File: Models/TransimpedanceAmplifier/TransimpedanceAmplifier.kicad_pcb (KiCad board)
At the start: 2 copper layers, 12 parts

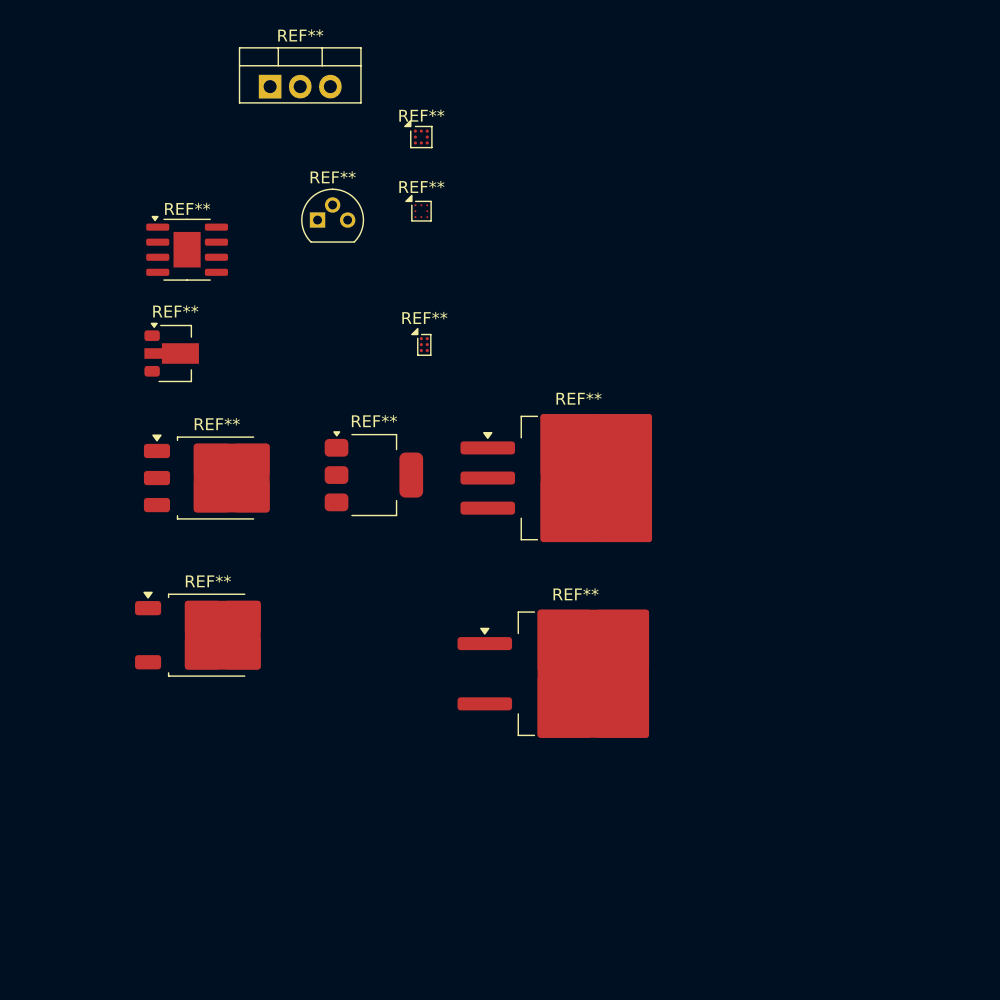
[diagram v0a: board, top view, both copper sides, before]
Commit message: Added KiCad libraries for more chips
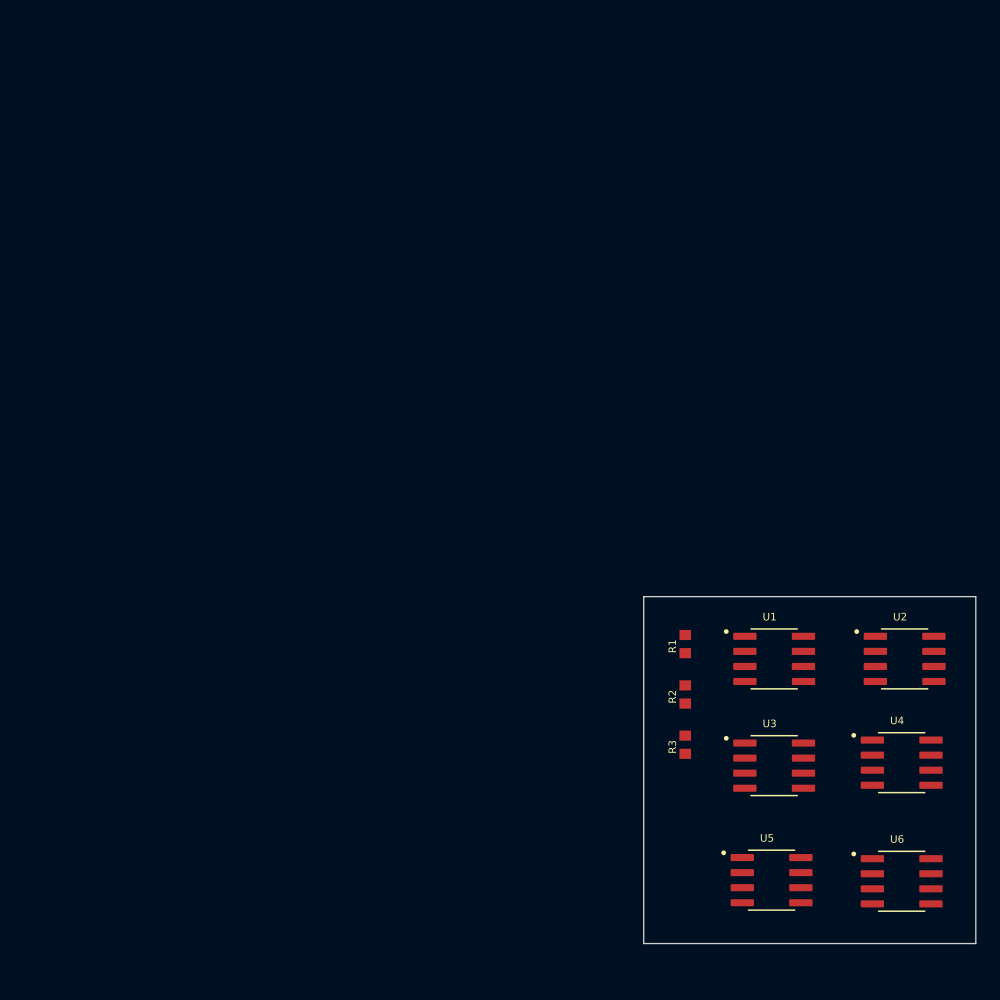
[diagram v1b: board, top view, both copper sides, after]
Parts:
- removed REF**: TO-252-3_TabPin2, Package_TO_SOT_SMD:TO-252-3_TabPin2
- removed REF**: TO-92, Package_TO_SOT_THT:TO-92
- removed REF**: TO-263-2, Package_TO_SOT_SMD:TO-263-2
- removed REF**: TO-263-3_TabPin2, Package_TO_SOT_SMD:TO-263-3_TabPin2
- removed REF**: SOIC-8-1EP_3.9x4.9mm_P1.27mm_EP2.29x3mm, Package_SO:SOIC-8-1EP_3.9x4.9mm_P1.27mm_EP2.29x3mm
- removed REF**: TO-220-3_Vertical, Package_TO_SOT_THT:TO-220-3_Vertical
- removed REF**: Texas_DSBGA-6_0.9x1.4mm_Layout2x3_P0.5mm, Package_BGA:Texas_DSBGA-6_0.9x1.4mm_Layout2x3_P0.5mm
- removed REF**: SOT-223, Package_TO_SOT_SMD:SOT-223
- removed REF**: Texas_DSBGA-8_1.5195x1.5195mm_Layout3x3_P0.5mm, Package_BGA:Texas_DSBGA-8_1.5195x1.5195mm_Layout3x3_P0.5mm
- removed REF**: Texas_DSBGA-8_1.43x1.41mm_Layout3x3_P0.5mm, Package_BGA:Texas_DSBGA-8_1.43x1.41mm_Layout3x3_P0.5mm
- removed REF**: TO-252-2, Package_TO_SOT_SMD:TO-252-2
- removed REF**: SOT-89-3, Package_TO_SOT_SMD:SOT-89-3
- added R1: 357, CRCW0603357RFKEA:RESC1508X50N, F.Cu at (153.8, 85.5)
- added R2: 499, CRCW0603499RFKEA:RESC1508X50N, F.Cu at (153.8, 89.8)
- added R3: 806, CRCW0603806RFKEA:RESC1508X50N, F.Cu at (153.8, 94.0)
- added U1: LM78L15ACMX, LM78L15ACMX_NOPB:SOIC127P599X175-8N, F.Cu at (161.2, 86.8)
- added U2: LM79L15ACMX, LM79L15ACMX_NOPB_NOPB:SOIC127P599X175-8N, F.Cu at (172.2, 86.8)
- added U3: LM78L05ACMX, LM78L05ACMX_NOPB:SOIC127P599X175-8N, F.Cu at (161.2, 95.8)
- added U4: LM79L05ACMX, LM79L05ACMX_NOPB:SOIC127P599X175-8N, F.Cu at (172.0, 95.5)
- added U5: LM78L05ACMX, LM78L05ACMX_NOPB:SOIC127P599X175-8N, F.Cu at (161.0, 105.4)
- added U6: LM79L05ACMX, LM79L05ACMX_NOPB:SOIC127P599X175-8N, F.Cu at (172.0, 105.5)
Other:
- board outline added: 28 x 29.2 mm

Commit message: Massive cleanup to the libraries for the transimpedance amplifier
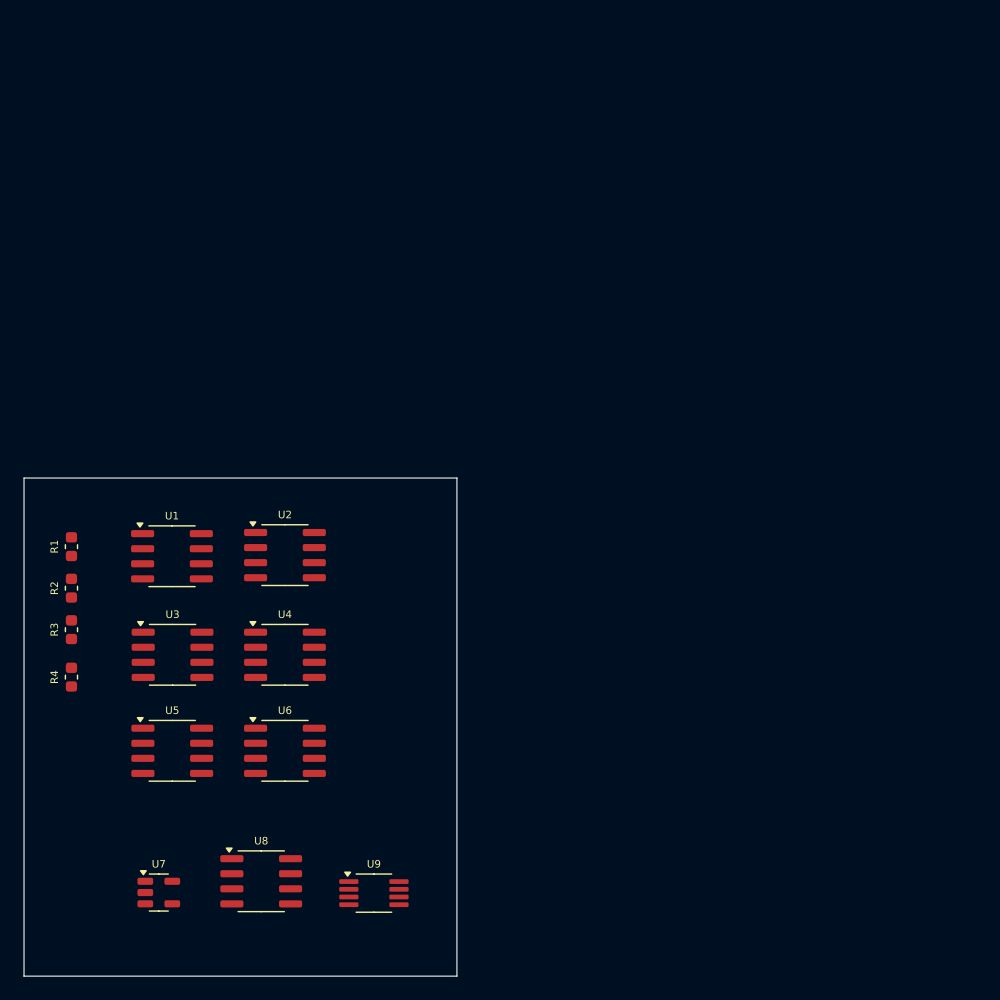
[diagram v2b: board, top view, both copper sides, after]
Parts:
- added R4: 330Meg, Generic_SMD_Fixed:R_0603_Fixed, F.Cu at (102.0, 88.3)
- added U7: AD8615AUJZ, Package_TO_SOT_SMD:TSOT-23-5, F.Cu at (109.4, 106.5)
- added U8: OP37GSZ, Package_SO:SOIC-8_3.9x4.9mm_P1.27mm, F.Cu at (118.0, 105.5)
- added U9: AD8676ARMZ, Package_SO:MSOP-8_3x3mm_P0.65mm, F.Cu at (127.5, 106.5)
- R1: footprint CRCW0603357RFKEA:RESC1508X50N -> Generic_SMD_Fixed:R_0603_Fixed
- R2: value 499 -> 806; footprint CRCW0603499RFKEA:RESC1508X50N -> Generic_SMD_Fixed:R_0603_Fixed
- R3: value 806 -> 499; footprint CRCW0603806RFKEA:RESC1508X50N -> Generic_SMD_Fixed:R_0603_Fixed
- U1: footprint LM78L15ACMX_NOPB:SOIC127P599X175-8N -> Package_SO:SOIC-8_3.9x4.9mm_P1.27mm
- U2: footprint LM79L15ACMX_NOPB_NOPB:SOIC127P599X175-8N -> Package_SO:SOIC-8_3.9x4.9mm_P1.27mm
- U3, U5: footprint LM78L05ACMX_NOPB:SOIC127P599X175-8N -> Package_SO:SOIC-8_3.9x4.9mm_P1.27mm
- U4, U6: footprint LM79L05ACMX_NOPB:SOIC127P599X175-8N -> Package_SO:SOIC-8_3.9x4.9mm_P1.27mm
- moved U6 53.2 mm to (120.0, 94.5)
- moved U2 53.0 mm to (120.0, 78.0)
- moved U4 52.8 mm to (120.0, 86.4)
- moved R3 52.7 mm to (102.0, 84.3)
- moved R2 52.5 mm to (102.0, 80.8)
- moved R1 52.4 mm to (102.0, 77.3)
- moved U5 51.7 mm to (110.5, 94.5)
- moved U3 51.6 mm to (110.5, 86.4)
- moved U1 51.5 mm to (110.5, 78.1)
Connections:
- U3 pad 4: unconnected-(U3-NC_4-Pad4) -> (no net)
- U3 pad 5: unconnected-(U3-NC_5-Pad5) -> (no net)
- U5 pad 4: unconnected-(U5-NC_4-Pad4) -> (no net)
- U5 pad 5: unconnected-(U5-NC_5-Pad5) -> (no net)
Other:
- board size 28 x 29.2 mm -> 36.5 x 42 mm
